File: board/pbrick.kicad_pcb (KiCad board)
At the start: 4 copper layers, 24 x 44 mm, 58 parts, among them J2 TC2030-IDC-NL, J3 U.FL2PIN, J4 QWIIC, M0 5055680471, M1 5055680471, Q1 SSM6J507NU, Q2 SSM6J507NU, U1 MIC5219-3.3YML-TR, U2 ADP3330ARTZ-5-RL7, U3 STUSB4500QTR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

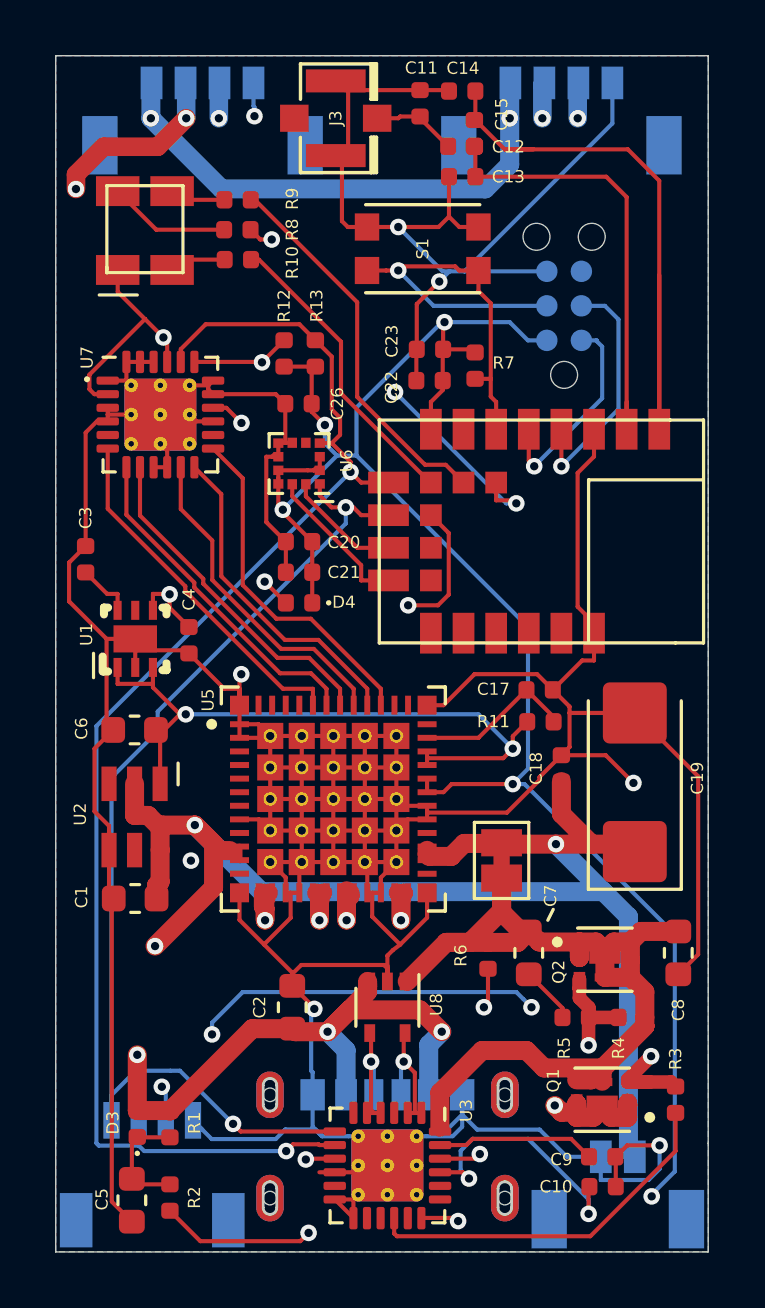
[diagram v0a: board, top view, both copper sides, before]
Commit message: Reverting to APP_PWM from board
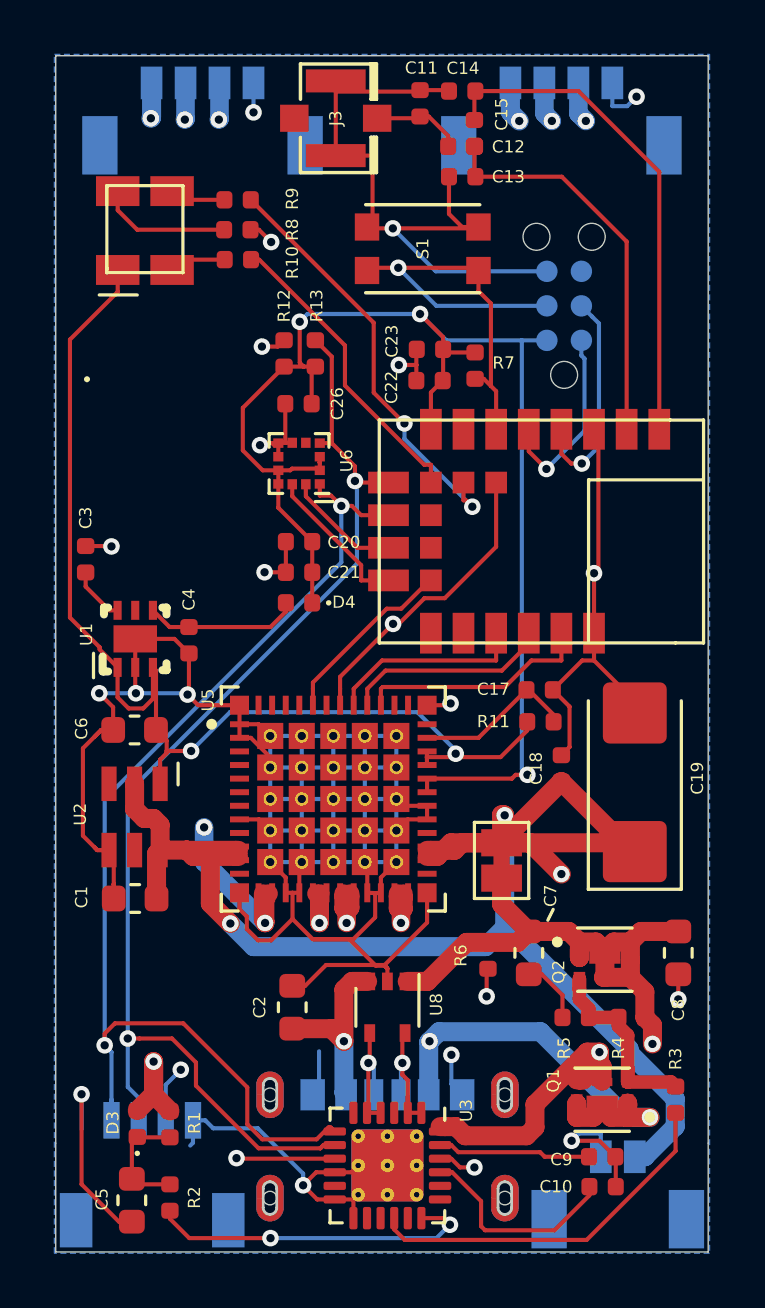
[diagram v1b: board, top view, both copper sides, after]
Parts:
- removed U7: PCA9624, Package_DFN_QFN:QFN-24-1EP_4x4mm_P0.5mm_EP2.65x2.65mm_ThermalVias
- J1: renamed from USB-C PD
- renumbered PWR to J5
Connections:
- J1 pad S2: (no net) -> Net-(J1-PadS1)
- J5 pad 3: (no net) -> Net-(J5-Pad3)
- J5 pad 4: (no net) -> Net-(J5-Pad4)
- U5 pad 39: /PCA9624_6 -> /P0.03
- U5 pad 40: /PCA9624_5 -> /P0.12
- U5 pad 41: /PCA9624_4 -> /P0.11
- U5 pad 42: /PCA9624_3 -> /P0.09
- U5 pad 43: /PCA9624_2 -> /P0.08
- U5 pad 44: /PCA9624_1 -> /P0.07
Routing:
- net GND: track 376.0 -> 194.1 mm, vias 7 -> 17
- net /P1.00: track 15.4 -> 0.00 mm, vias 2 -> 0
- net /PCA9624_1: track 13.2 -> 0.00 mm
- net /PCA9624_6: track 12.7 -> 0.00 mm
- net /PCA9624_3: track 12.5 -> 0.00 mm
- net /PCA9624_2: track 12.5 -> 0.00 mm
- net /PCA9624_5: track 12.1 -> 0.00 mm
- net /PCA9624_4: track 12.1 -> 0.00 mm
- net /P0.09: track 16.0 -> 28.0 mm, vias 3 -> 2
- net 3.3V: track 102.8 -> 91.6 mm, vias 9 -> 5
- net /P0.03: track 0.00 -> 8.68 mm
- net /P0.12: track 0.00 -> 7.62 mm
- net /P0.11: track 0.00 -> 7.28 mm
- net VSS: track 40.4 -> 33.3 mm, vias 0 -> 2
- net /P0.07: track 0.00 -> 6.73 mm
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- removed copper zone on M.Cu, net VDD

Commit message: Wrong board wiring again...
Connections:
- J1 pad S2: Net-(J1-PadS1) -> (no net)
- U1 pad GND: GND -> (no net)
- U5 pad 42: /P0.09 -> /P1.09
- U5 pad 43: /P0.08 -> /P1.08
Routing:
- net /P1.09: track 0.00 -> 6.50 mm
- net /P1.08: track 0.00 -> 5.27 mm
- net /P0.03: track 8.68 -> 12.0 mm
- net /P0.07: track 6.73 -> 9.93 mm, vias 0 -> 2
- net /P0.09: track 28.0 -> 24.9 mm
- net /P0.12: track 7.62 -> 9.99 mm
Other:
- board text added: "PBRICK - PROTEUS III - REVISION XII"
- board text removed: "PBRICK - PROTEUS III - REVISION X"

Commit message: Minor board update
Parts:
- JP1: footprint Jumper:SolderJumper-2_P1.3mm_Bridged_Pad1.0x1.5mm -> Jumper:SolderJumper-2_P1.3mm_Open_Pad1.0x1.5mm
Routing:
- net VDD: track 110.4 -> 108.8 mm, vias 5 -> 4
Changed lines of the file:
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@@
     (thickness 1.6)
     (drawings 15)
-    (tracks 939)
+    (tracks 933)
     (zones 0)
     (modules 57)
@@
     (add_net "Net-(Q1-Pad3)")
   )
+  (module Jumper:SolderJumper-2_P1.3mm_Open_Pad1.0x1.5mm (layer F.Cu)
+    (at 136.4 119.6 90)
+    (descr "SMD Solder Jumper, 1x1.5mm Pads, 0.3mm gap, open")
+    (tags "solder jumper open")
+    (attr virtual)
+    (fp_text reference JP1 (at -0.65 1.8 90) (layer F.SilkS) hide
+      (effects (font (size 0.45 0.45) (thickness 0.1125)))
+    )
+    (fp_text value SolderJumper_2_Bridged (at 0 1.9 90) (layer F.Fab) hide
+      (effects (font (size 1 1) (thickness 0.15)))
+    )
+    (fp_line (start 1.65 1.25) (end -1.65 1.25) (layer F.CrtYd) (width 0.05))
+    (fp_line (start 1.65 1.25) (end 1.65 -1.25) (layer F.CrtYd) (width 0.05))
+    (fp_line (start -1.65 -1.25) (end -1.65 1.25) (layer F.CrtYd) (width 0.05))
+    (fp_line (start -1.65 -1.25) (end 1.65 -1.25) (layer F.CrtYd) (width 0.05))
+    (fp_line (start -1.4 -1) (end 1.4 -1) (layer F.SilkS) (width 0.12))
+    (fp_line (start 1.4 -1) (end 1.4 1) (layer F.SilkS) (width 0.12))
+    (fp_line (start 1.4 1) (end -1.4 1) (layer F.SilkS) (width 0.12))
+    (fp_line (start -1.4 1) (end -1.4 -1) (layer F.SilkS) (width 0.12))
+    (pad 1 smd rect (at -0.65 0 90) (size 1 1.5) (layers F.Cu F.Mask)
+      (net 62 VSS))
+    (pad 2 smd rect (at 0.65 0 90) (size 1 1.5) (layers F.Cu F.Mask)
+      (net 1 VDD))
+  )
   (module "Common:IC_TB67H420FTG(O,EL)" (layer F.Cu)
     (at 130.21 117.34)
@@
     )
   )
-  (module Jumper:SolderJumper-2_P1.3mm_Bridged_Pad1.0x1.5mm (layer F.Cu)
-    (at 136.4 119.6 90)
-    (descr "SMD Solder Jumper, 1x1.5mm Pads, 0.3mm gap, bridged with 1 copper strip")
-    (tags "solder jumper open")
-    (attr virtual)
-    (fp_text reference JP1 (at -0.65 1.8 90) (layer F.SilkS) hide
-      (effects (font (size 0.45 0.45) (thickness 0.1125)))
-    )
-    (fp_text value SolderJumper_2_Bridged (at 0 1.9 90) (layer F.Fab) hide
-      (effects (font (size 1 1) (thickness 0.15)))
-    )
-    (fp_line (start -1.4 1) (end -1.4 -1) (layer F.SilkS) (width 0.12))
-    (fp_line (start 1.4 1) (end -1.4 1) (layer F.SilkS) (width 0.12))
-    (fp_line (start 1.4 -1) (end 1.4 1) (layer F.SilkS) (width 0.12))
-    (fp_line (start -1.4 -1) (end 1.4 -1) (layer F.SilkS) (width 0.12))
-    (fp_line (start -1.65 -1.25) (end 1.65 -1.25) (layer F.CrtYd) (width 0.05))
-    (fp_line (start -1.65 -1.25) (end -1.65 1.25) (layer F.CrtYd) (width 0.05))
-    (fp_line (start 1.65 1.25) (end 1.65 -1.25) (layer F.CrtYd) (width 0.05))
-    (fp_line (start 1.65 1.25) (end -1.65 1.25) (layer F.CrtYd) (width 0.05))
-    (fp_poly (pts (xy -0.25 -0.3) (xy 0.25 -0.3) (xy 0.25 0.3) (xy -0.25 0.3)) (layer F.Cu) (width 0))
-    (pad 2 smd rect (at 0.65 0 90) (size 1 1.5) (layers F.Cu F.Mask)
-      (net 1 VDD))
-    (pad 1 smd rect (at -0.65 0 90) (size 1 1.5) (layers F.Cu F.Mask)
-      (net 62 VSS))
-  )
   (module Connectors:1X04_1MM_RA (layer B.Cu)
     (at 123.55 129.16 180)
@@
   (via (at 137.05 92.4) (size 0.6096) (layers F.Cu B.Cu) (net 1))
   (via (at 123.5 92.3) (size 0.6096) (layers F.Cu B.Cu) (net 1))
-  (via (at 138.6 120.1) (size 0.6096) (drill 0.3048) (layers F.Cu B.Cu) (net 1))
-  (segment (start 137.45 118.95) (end 138.6 120.1) (width 0.7) (layer F.Cu) (net 1))
   (segment (start 136.4 118.95) (end 137.45 118.95) (width 0.7) (layer F.Cu) (net 1))
   (segment (start 129.2 105.7625) (end 129.2 106.2043) (width 0.1524) (layer F.Cu) (net 2))
@@
   (segment (start 122.051 128.408) (end 122.051 126.651) (width 0.1524) (layer B.Cu) (net 33))
   (segment (start 122.051 126.651) (end 121.8 126.4) (width 0.1524) (layer B.Cu) (net 33))
-  (segment (start 130.187 129.495) (end 130.1875 129.495) (width 0.1524) (layer F.Cu) (net 33))
   (segment (start 130.1875 129.495) (end 130.2625 129.57) (width 0.1524) (layer F.Cu) (net 33))
   (segment (start 130.187 129.495) (end 130.262 129.57) (width 0.1524) (layer F.Cu) (net 33))
-  (segment (start 121.8 126.4) (end 121.8 125.969) (width 0.1524) (layer F.Cu) (net 33))
-  (segment (start 121.8 125.969) (end 122.178 125.591) (width 0.1524) (layer F.Cu) (net 33))
-  (segment (start 122.178 125.591) (end 124.691 125.591) (width 0.1524) (layer F.Cu) (net 33))
-  (segment (start 124.691 125.591) (end 127.046 127.946) (width 0.1524) (layer F.Cu) (net 33))
-  (segment (start 127.046 127.946) (end 127.046 129.305) (width 0.1524) (layer F.Cu) (net 33))
-  (segment (start 127.046 129.305) (end 127.599 129.859) (width 0.1524) (layer F.Cu) (net 33))
-  (segment (start 127.599 129.859) (end 129.596 129.859) (width 0.1524) (layer F.Cu) (net 33))
-  (segment (start 129.596 129.859) (end 130.035 129.42) (width 0.1524) (layer F.Cu) (net 33))
-  (segment (start 130.035 129.42) (end 130.112 129.42) (width 0.1524) (layer F.Cu) (net 33))
-  (segment (start 130.112 129.42) (end 130.187 129.495) (width 0.1524) (layer F.Cu) (net 33))
   (segment (start 122.051 128.408) (end 122.0514 128.4084) (width 0.1524) (layer B.Cu) (net 33))
   (segment (start 122.0514 128.4084) (end 122.0514 129.16) (width 0.1524) (layer B.Cu) (net 33))
@@
   (via (at 130.5053 106.5592) (size 0.6096) (layers F.Cu B.Cu) (net 33))
   (via (at 121.8 126.4) (size 0.6096) (layers F.Cu B.Cu) (net 33))
+  (segment (start 121.8 125.969) (end 121.8 126.4) (width 0.1524) (layer F.Cu) (net 33))
+  (segment (start 122.178 125.591) (end 121.8 125.969) (width 0.1524) (layer F.Cu) (net 33))
+  (segment (start 124.691 125.591) (end 122.178 125.591) (width 0.1524) (layer F.Cu) (net 33))
+  (segment (start 127.046 129.305226) (end 127.046 127.946) (width 0.1524) (layer F.Cu) (net 33))
+  (segment (start 127.310774 129.57) (end 127.046 129.305226) (width 0.1524) (layer F.Cu) (net 33))
+  (segment (start 127.046 127.946) (end 124.691 125.591) (width 0.1524) (layer F.Cu) (net 33))
+  (segment (start 130.2625 129.57) (end 127.310774 129.57) (width 0.1524) (layer F.Cu) (net 33))
   (segment (start 131.0069 105.6425) (end 131.0807 105.7163) (width 0.1524) (layer B.Cu) (net 34))
   (segment (start 131.0807 105.7163) (end 131.0807 108.6834) (width 0.1524) (layer B.Cu) (net 34))

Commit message: Minor wire change
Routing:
- net Net-(C5-Pad1): track 4.32 -> 6.05 mm
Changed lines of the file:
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@@
     (thickness 1.6)
     (drawings 15)
-    (tracks 933)
+    (tracks 934)
     (zones 0)
     (modules 57)
@@
   (segment (start 124.2 129.785) (end 123.015 129.785) (width 0.1524) (layer F.Cu) (net 28))
   (segment (start 123.015 129.785) (end 123 129.77) (width 0.1524) (layer F.Cu) (net 28))
+  (segment (start 124.2 129.785) (end 124.2 131.515) (width 0.1524) (layer F.Cu) (net 28))
   (segment (start 137.4 123.7875) (end 137.4 123.788) (width 0.1524) (layer F.Cu) (net 29))
   (segment (start 137.4 123.788) (end 137.875 123.788) (width 0.1524) (layer F.Cu) (net 29))

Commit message: Updating Board layout, pcb, board definition
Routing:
- net 3.3V: track 91.6 -> 111.8 mm, vias 5 -> 6
- net /M0_0: track 38.9 -> 43.1 mm
- net /M1_0: track 36.0 -> 39.0 mm
- net VDD: track 108.8 -> 111.0 mm
- net /M1_1: track 35.0 -> 36.7 mm
- net /M0_1: track 40.3 -> 39.2 mm
- net GND: vias 17 -> 16

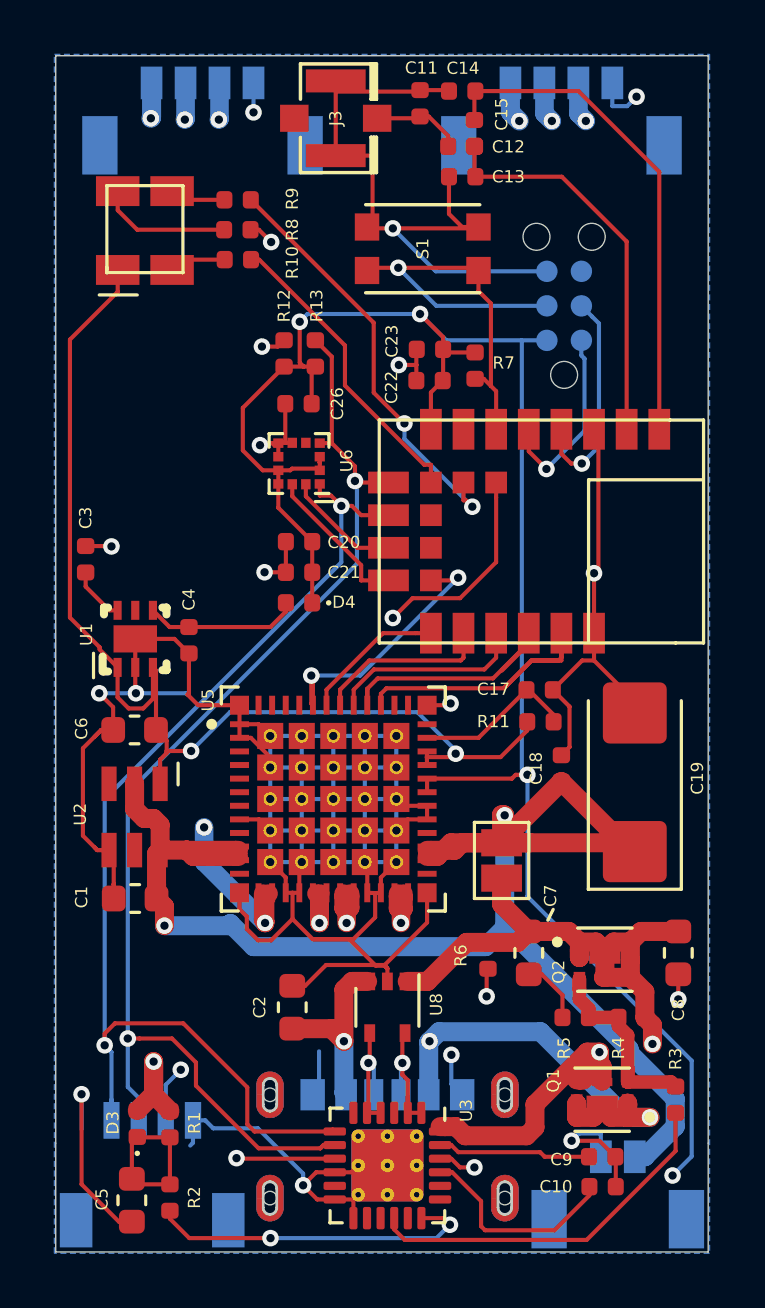
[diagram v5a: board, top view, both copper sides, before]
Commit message: Updating board layout to align with other PF modules - Swapped GND and VDD on M0 and M0 to avoid wire crossing in cable wiring (external) - Swapped M1_0 and M1_1 to eliminate trace crossover (will solve in software) - VSS => VDD is disconnected by default. Solder to power board via VSS (STUSB4500, USB-C PD power).     - This allows the board to be exclusivly powered by J5 due to parts shortage     - Additionally, a diode can be placed VSS => VDD to prevent VDD from backflowing (optional, VSS => VDD has GND short protection via Mosfets and chipset in STUSB4500). - FLooded VDD on M.Cu plane
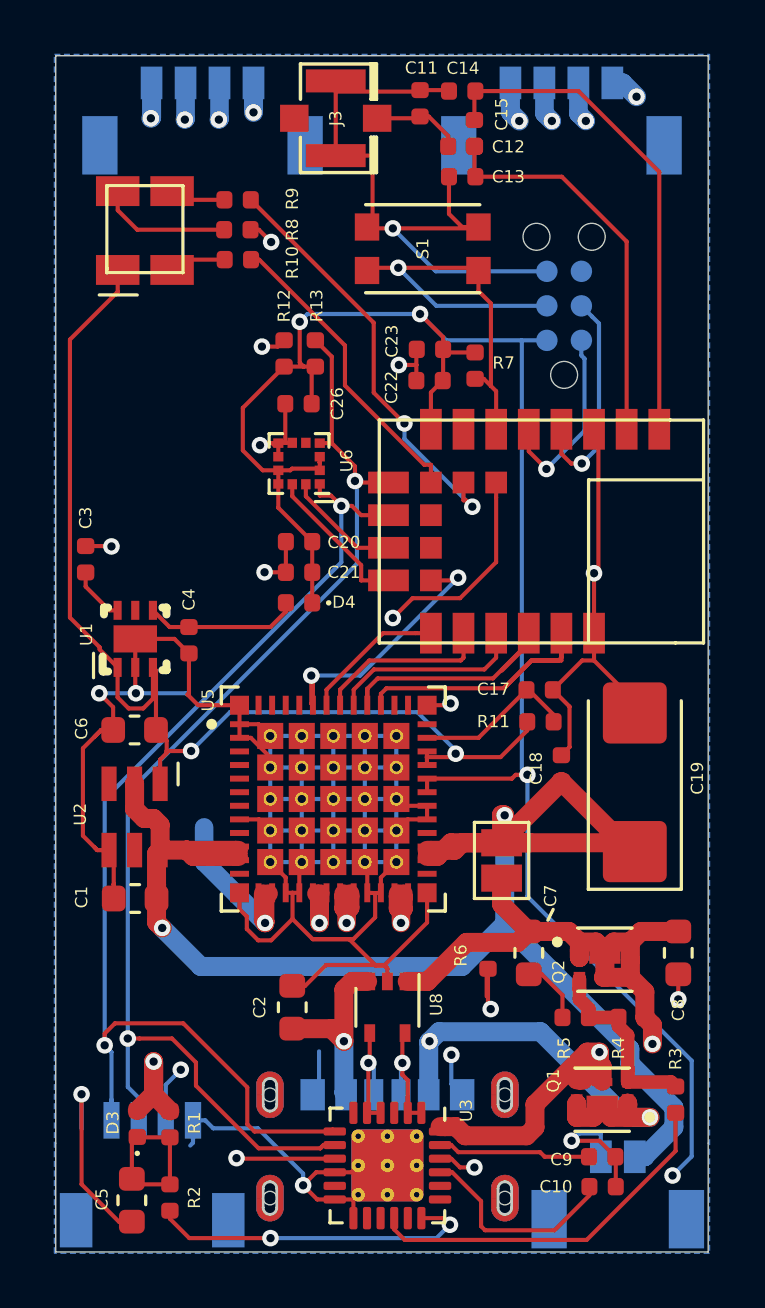
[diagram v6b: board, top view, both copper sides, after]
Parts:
- C20: value 10nF 0402 -> 100nF 0402
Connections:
- M0 pad 1: VDD -> GND
- M0 pad 4: GND -> VDD
- M1 pad 1: VDD -> GND
- M1 pad 2: /M1_1 -> /M1_0
- M1 pad 3: /M1_0 -> /M1_1
- M1 pad 4: GND -> VDD
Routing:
- net GND: track 194.1 -> 240.4 mm
- net VDD: track 111.0 -> 100.8 mm
- net /M1_1: track 36.7 -> 39.9 mm, vias 3 -> 2
- net /DISCH: track 17.3 -> 18.4 mm
- net /M1_0: track 39.0 -> 39.8 mm
- net 3.3V: track 111.8 -> 111.1 mm
- added copper zone on M.Cu, net VDD
- removed copper zone on M.Cu, net GND
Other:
- board text added: "PBRICK - PROTEUS III - REVISION XIII"
- board text removed: "PBRICK - PROTEUS III - REVISION XII"
